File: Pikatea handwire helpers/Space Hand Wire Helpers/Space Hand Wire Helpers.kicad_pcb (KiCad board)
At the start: 2 copper layers, 104.9 x 20 mm, 3 parts

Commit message: update andwire gerbers
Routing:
- net Net-(D1-Pad1): track 29.0 -> 110.3 mm
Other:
- board size 104.9 x 20 mm -> 109.9 x 20 mm

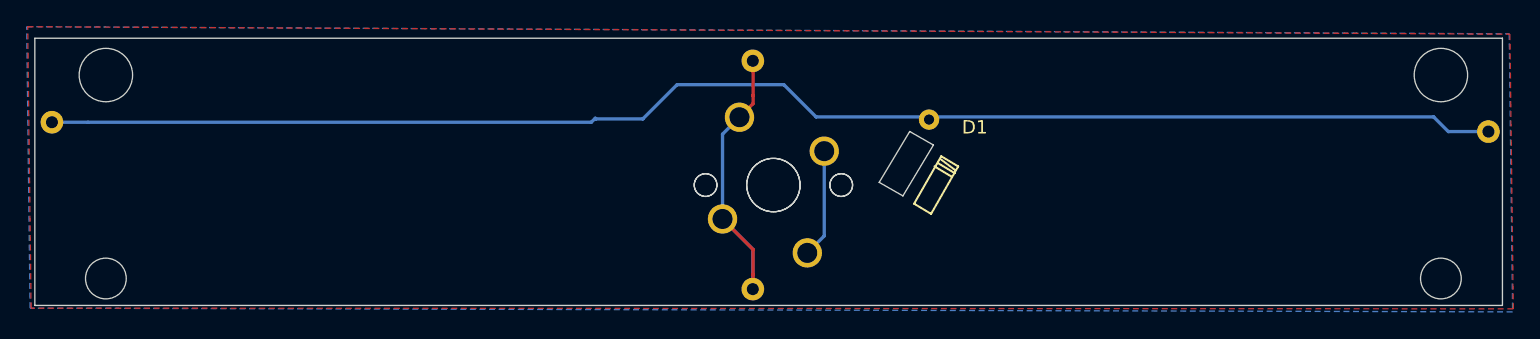
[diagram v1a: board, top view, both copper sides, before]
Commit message: update handwire helpers
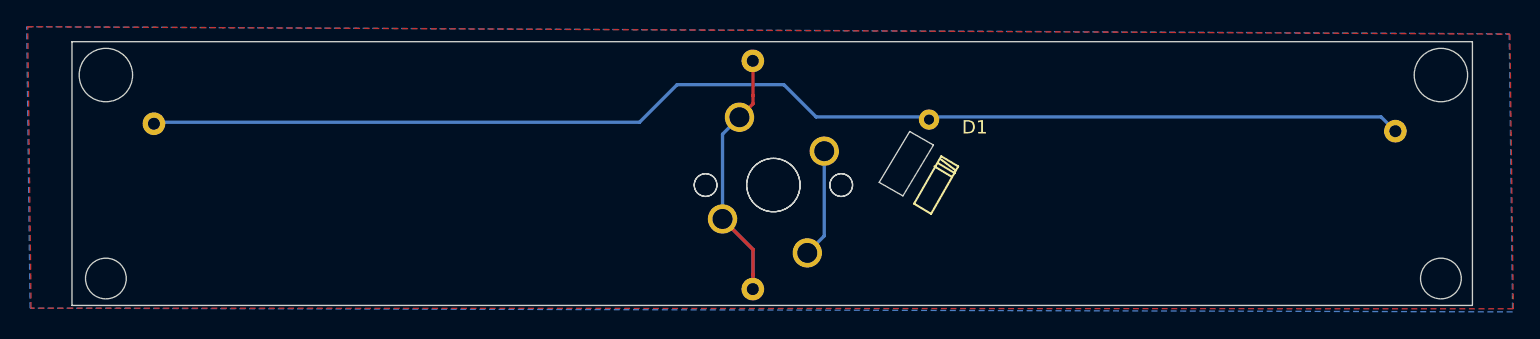
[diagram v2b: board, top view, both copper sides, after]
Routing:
- net Net-(D1-Pad1): track 110.3 -> 95.6 mm
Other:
- board size 109.9 x 20 mm -> 104.9 x 19.8 mm
- net class Default removed
